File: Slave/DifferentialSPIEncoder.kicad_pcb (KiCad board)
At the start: 2 copper layers, 35.6 x 26.6 mm, 30 parts, among them J1 Conn_01x05_Male, J2 8P8C_Shielded, U1 TLV71333PDBV, U2 AS5048A, U3 MAX485E, U4 MAX485E, U5 MAX485E

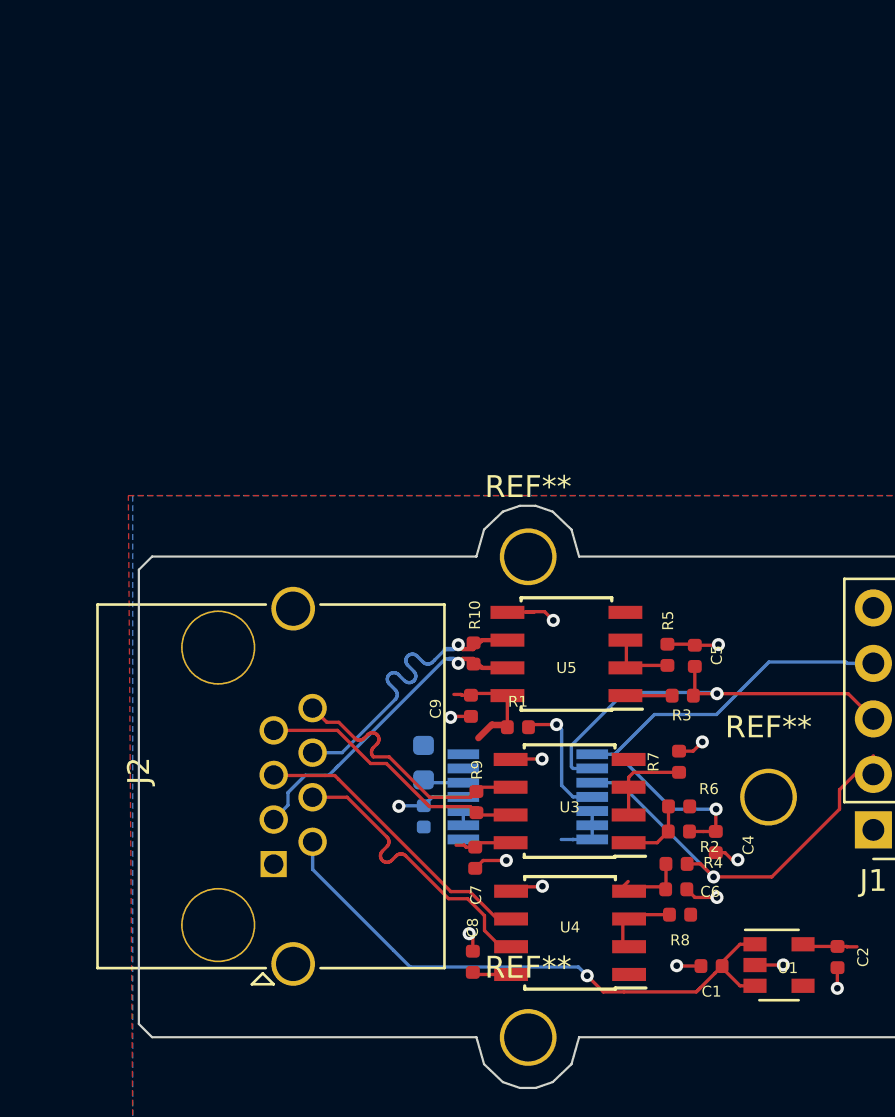
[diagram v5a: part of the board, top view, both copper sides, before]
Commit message: Update slave schematic with changes from #2
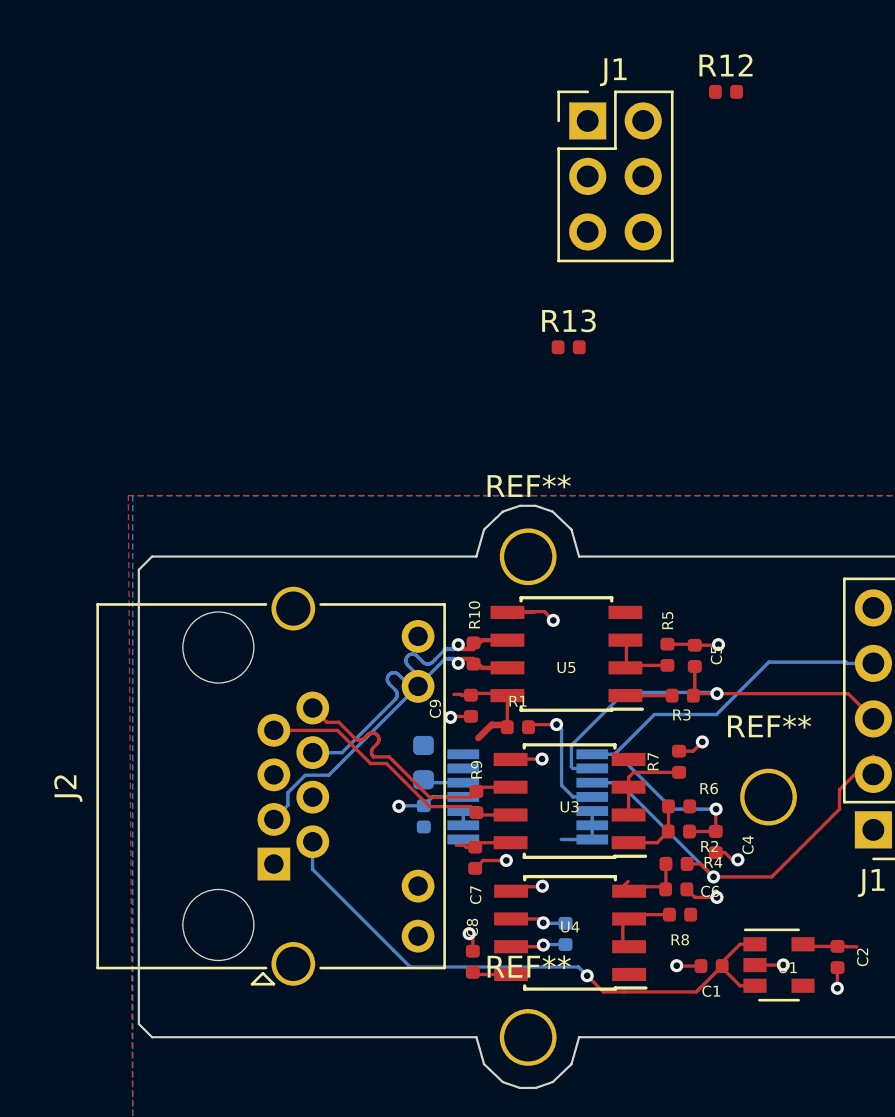
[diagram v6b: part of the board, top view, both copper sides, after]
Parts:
- added J1: Debug, Connector_PinHeader_2.54mm:PinHeader_2x03_P2.54mm_Vertical, F.Cu at (115.8, 35.1)
- added R11: 120, Resistor_SMD:R_0402_1005Metric, B.Cu at (114.8, 72.3)
- added R12: 220, Resistor_SMD:R_0402_1005Metric, F.Cu at (122.2, 33.7)
- added R13: 220, Resistor_SMD:R_0402_1005Metric, F.Cu at (115.0, 45.4)
- C4, C5, C6: value C -> 2.2pF
- J2: value 8P8C_Shielded -> 8P8C_LED_Shielded; footprint Connector_RJ:RJ45_Amphenol_RJHSE5380 -> Connector_RJ:RJ45_Amphenol_RJHSE538X
- R1: value 10k -> 1k
- R2, R3, R4: value R -> 1k
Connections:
- net Net-(R1-Pad2) renamed /MOSI
- U2 pad 10: GND -> Net-(U2-Pad10)
- U2 pad 6: GND -> Net-(U2-Pad6)
- U2 pad 7: GND -> Net-(U2-Pad7)
- U2 pad 8: GND -> Net-(U2-Pad8)
- U2 pad 9: GND -> Net-(U2-Pad9)
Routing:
- net /MISO_-: track 13.6 -> 2.53 mm, vias 0 -> 1
- net /MISO_+: track 13.6 -> 2.57 mm, vias 0 -> 1
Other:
- net class Default: via_dia 0.8 -> 0.6; via_drill 0.4 -> 0.3

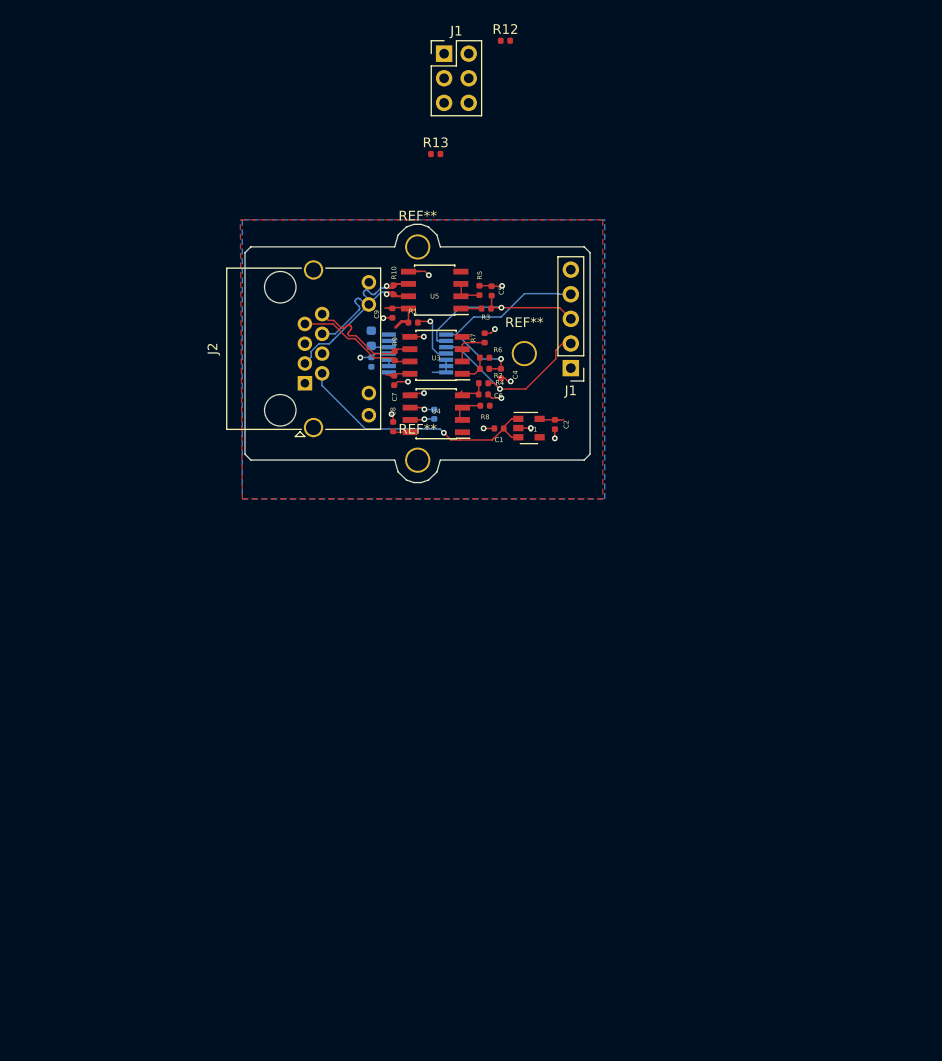
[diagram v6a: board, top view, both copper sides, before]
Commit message: Fit slave to AMT102 footprint
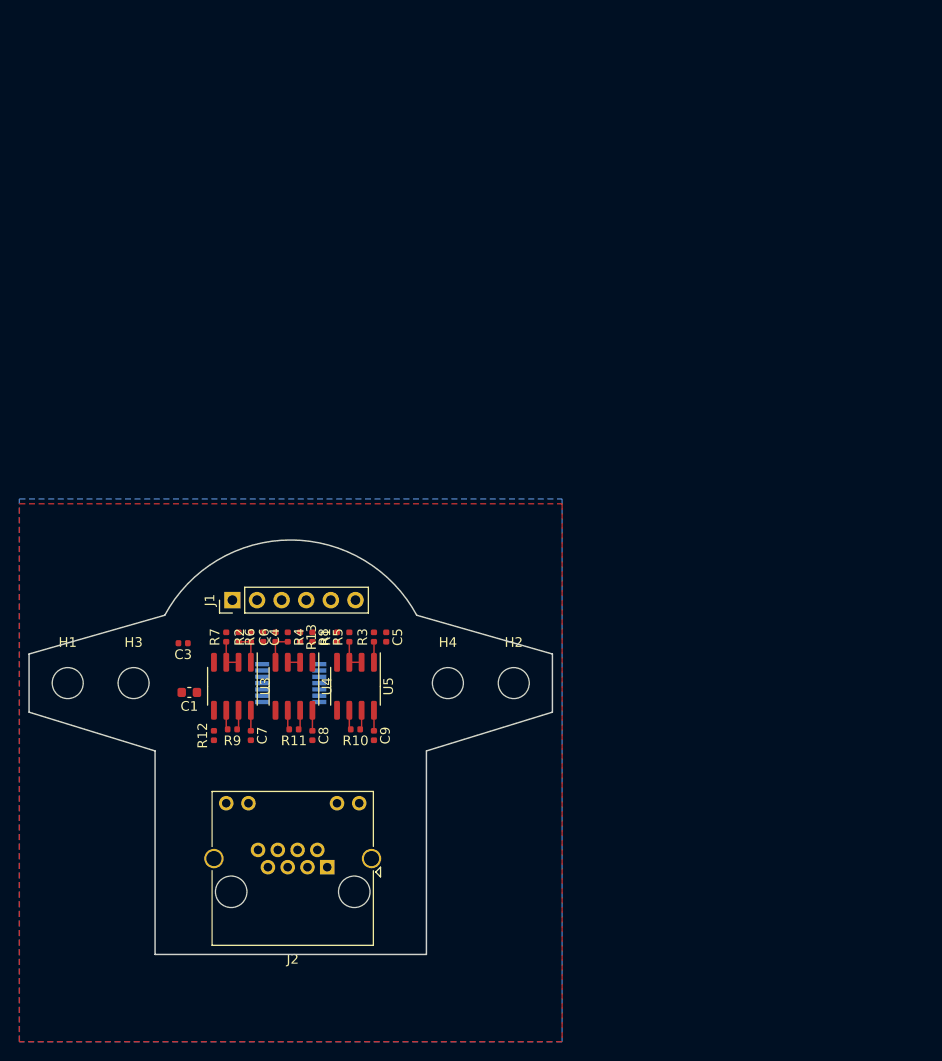
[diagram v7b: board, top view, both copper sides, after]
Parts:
- removed the C1 at (108.3, 64.4)
- removed the C1 at (121.5, 73.7)
- removed C2: 100nF, Capacitor_SMD:C_0402_1005Metric
- removed the J1 at (115.8, 35.1)
- removed the J1 at (128.9, 67.5)
- removed REF** (x3): MountingHole_MINE, MountingHole:MountingHole_MINE
- removed U1: TLV71333PDBV, Package_TO_SOT_SMD:SOT-23-5
- added C1: 10uF, Capacitor_SMD:C_0603_1608Metric, F.Cu at (89.5, 101.0)
- added H1: MountingHole, MountingHole:MountingHole_3.2mm_M3, F.Cu at (77.0, 100.0)
- added H2: MountingHole, MountingHole:MountingHole_3.2mm_M3, F.Cu at (123.0, 100.0)
- added H3: MountingHole, MountingHole:MountingHole_3.2mm_M3, F.Cu at (83.8, 100.0)
- added H4: MountingHole, MountingHole:MountingHole_3.2mm_M3, F.Cu at (116.2, 100.0)
- added J1: Debug, Connector_PinHeader_2.54mm:PinHeader_1x06_P2.54mm_Vertical, F.Cu at (94.0, 91.4)
- C3, R11: moved to F.Cu
- U3, U4, U5: value MAX485E -> SN65HVD06D
- moved R12 77.7 mm to (92.1, 105.4), turned to 90 degrees
- moved R13 51.8 mm to (101.0, 95.2), turned to 270 degrees
- moved J2 50.0 mm to (103.8, 119.0), turned to 180 degrees
- moved R10 45.5 mm to (106.7, 104.8), turned to 180 degrees
- moved C9 43.6 mm to (108.6, 105.4)
- moved R9 42.0 mm to (94.0, 104.8), turned to 180 degrees
- moved U5 41.7 mm to (106.7, 100.3), turned to 270 degrees
- moved R7 40.8 mm to (93.3, 95.2)
- moved U3 40.1 mm to (94.0, 100.3), turned to 270 degrees
- moved C7 39.5 mm to (95.9, 105.4)
- moved R6 38.4 mm to (94.6, 95.2), turned to 270 degrees
- moved R5 38.2 mm to (106.0, 95.2)
- moved C5 37.3 mm to (109.9, 95.2), turned to 270 degrees
- moved R2 36.7 mm to (95.9, 95.2), turned to 90 degrees
- moved C4 36.6 mm to (97.2, 95.2)
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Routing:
- net +5V: track 39.9 -> 6.36 mm, vias 2 -> 0
- net ~CSn: track 22.7 -> 0.00 mm, vias 1 -> 0
- net GND: track 22.5 -> 0.00 mm, vias 13 -> 0
- net CLK: track 19.8 -> 0.00 mm, vias 1 -> 0
- net MISO: track 18.9 -> 0.00 mm, vias 1 -> 0
- net /CLK_-: track 14.5 -> 2.03 mm, vias 1 -> 0
- net /CLK_+: track 14.2 -> 2.03 mm, vias 1 -> 0
- net /CS_-: track 12.9 -> 2.03 mm
- net /CS_+: track 12.6 -> 2.03 mm
- net /MOSI: track 5.79 -> 0.00 mm, vias 1 -> 0
- net +3V3: track 2.77 -> 0.00 mm
- net Net-(R8-Pad2): track 3.41 -> 1.27 mm
- net V3cap: track 1.87 -> 0.00 mm
- net Net-(R7-Pad1): track 4.13 -> 3.39 mm
- net /MISO_+: track 2.57 -> 2.03 mm, vias 1 -> 0
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- added copper zone on B.Cu, net +5V
- added copper zone on F.Cu, net GND
- removed copper zone on F.Cu, net +5V
- removed copper zone on B.Cu, net GND
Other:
- board size 35.6 x 26.6 mm -> 54 x 42.8 mm

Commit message: Finish slave layout
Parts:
- C1, C3: moved to B.Cu
- J1: footprint Connector_PinHeader_2.54mm:PinHeader_1x06_P2.54mm_Vertical -> Connector_PinHeader_2.54mm:PinHeader_2x03_P2.54mm_Vertical
- moved C3 14.8 mm to (99.7, 106.0), turned to 270 degrees
- moved R13 14.7 mm to (104.8, 109.5), turned to 90 degrees
- moved C1 10.2 mm to (98.4, 106.0), turned to 270 degrees
- moved J1 9.25 mm to (102.9, 88.9), turned to 270 degrees
- moved R12 4.38 mm to (93.3, 109.6)
- turned U2 to 270 degrees
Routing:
- net MISO: track 0.00 -> 27.6 mm, vias 0 -> 2
- net CLK: track 0.00 -> 24.8 mm, vias 0 -> 1
- net Net-(J2-PadSH): track 0.00 -> 17.8 mm
- net /CLK_+: track 2.03 -> 18.8 mm, vias 0 -> 1
- net /CLK_-: track 2.03 -> 18.8 mm, vias 0 -> 1
- net /CS_+: track 2.03 -> 17.8 mm
- net /CS_-: track 2.03 -> 17.8 mm
- net +5V: track 6.36 -> 21.2 mm, vias 0 -> 7
- net /MISO_-: track 2.03 -> 16.3 mm
- net /MISO_+: track 2.03 -> 16.3 mm
- net ~CSn: track 0.00 -> 12.9 mm, vias 0 -> 1
- net /MOSI: track 0.00 -> 12.6 mm, vias 0 -> 1
- net V3cap: track 0.00 -> 9.83 mm, vias 0 -> 1
- net GND: track 0.00 -> 8.54 mm, vias 0 -> 3
- net Net-(R8-Pad2): track 1.27 -> 3.92 mm
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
